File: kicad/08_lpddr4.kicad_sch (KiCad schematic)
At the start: 42 parts, among them U501 Ti135N484I3, U801 H9HCNNN8KUMLHR-NME

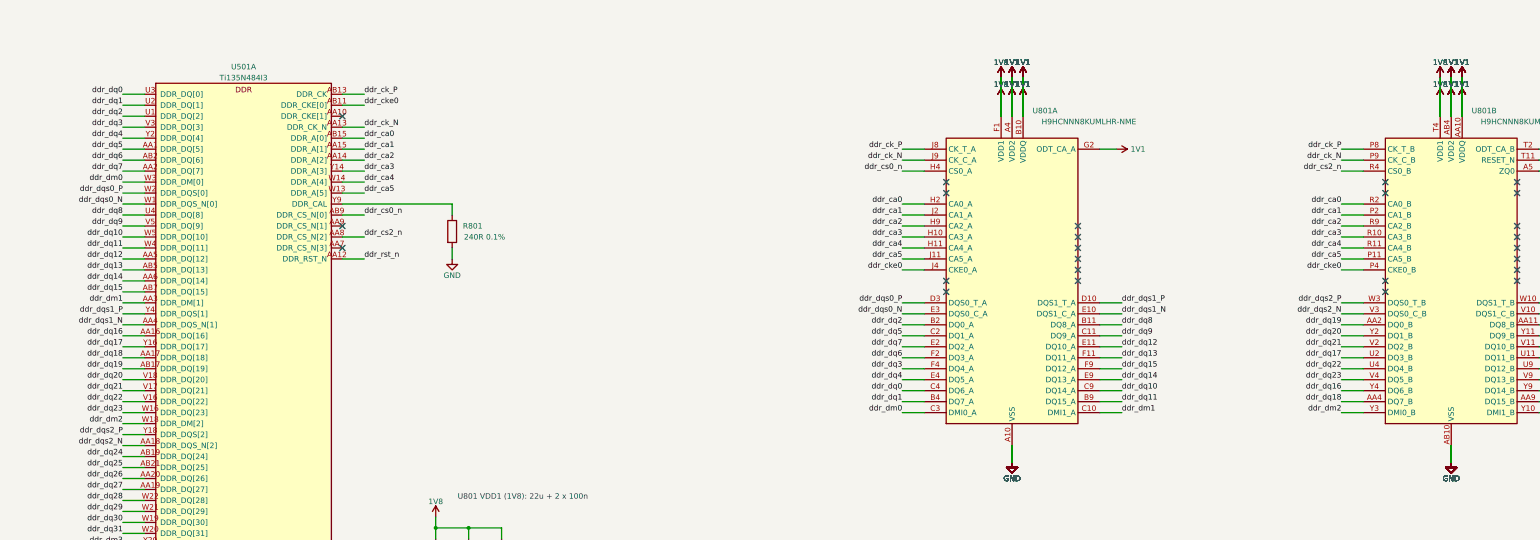
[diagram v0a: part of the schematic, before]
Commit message: LPDDR4 hand routing: Agilex DRAM escape copied, byte lanes routed, DQ swizzle by hand
- U801 decoupling = the Agilex U12 set (sheet 08: 29 x 100n 0201, 22u/1u 0402, LCSC from the
  Agilex card), placed at the Agilex positions on the same via pairs; R802 (ZQ) at R43's spot;
  CA/CKE T-branches on B.Cu copied (tools/ddr/copy_dram_escape.py)
- LPDDR4 vias not on a BGA ball removed (T-branch centre vias kept)
- Schematic: #PWR/#FLG references made unique per sheet (prefix = sheet number); the
  duplicates blocked Update PCB from Schematic
- DQ swizzle now edited by hand in the schematic (bytes 0 and 2); efinity/pinplan/lpddr4_swizzle.json
  is not updated yet
- Byte lanes routed by hand (work in progress)

Known open (WIP): byte 2 - ddr_dq22 on two U501 balls (AA16, W16), ddr_dq21 has no U501 ball;
DRC shows 2 shorts at U501 Y16/W16 (dq21/dq17 tracks).

Co-Authored-By: Claude Opus 5.5 <noreply@anthropic.com>
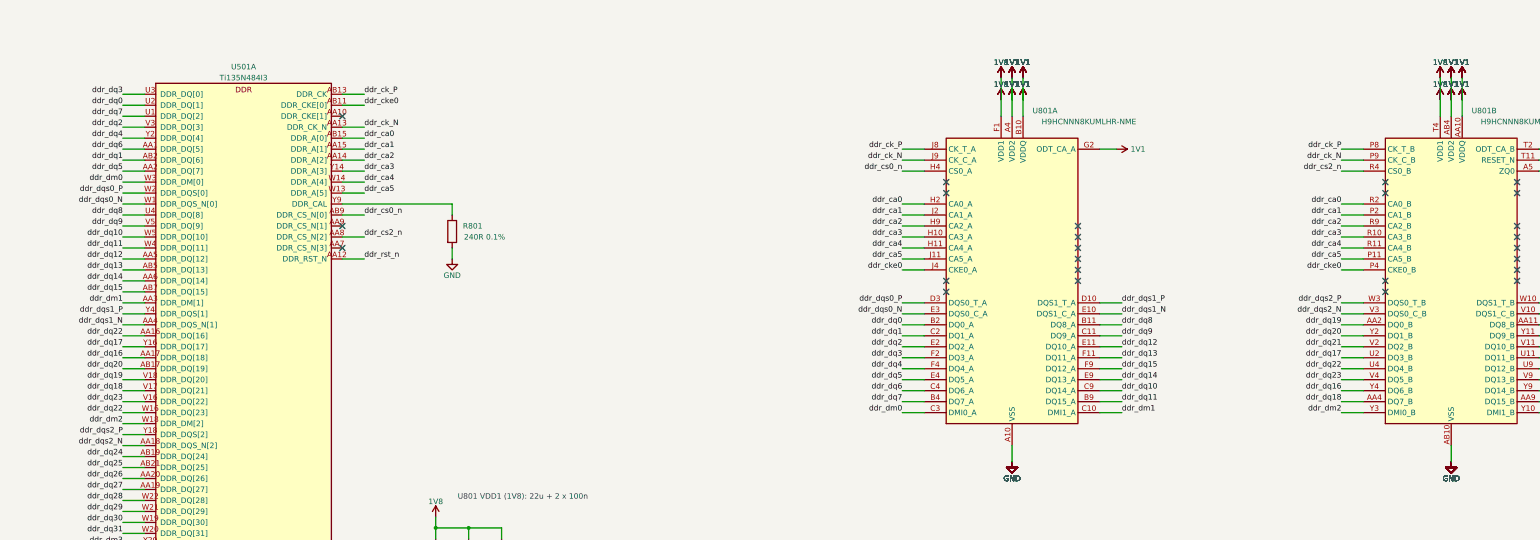
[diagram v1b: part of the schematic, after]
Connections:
- net ddr_dq0: now also U501.U2 (DDR_DQ[1]), U801.B2 (DQ0_A); no longer U501.U3 (DDR_DQ[0]), U801.C4 (DQ6_A)
- net ddr_dq1: now also U501.AB2 (DDR_DQ[6]), U801.C2 (DQ1_A); no longer U501.U2 (DDR_DQ[1]), U801.B4 (DQ7_A)
- net ddr_dq16: now also U501.AA17 (DDR_DQ[18]); no longer U501.AA16 (DDR_DQ[16])
- net ddr_dq18: now also U501.V17 (DDR_DQ[21]); no longer U501.AA17 (DDR_DQ[18])
- net ddr_dq19: now also U501.V18 (DDR_DQ[20]); no longer U501.AB17 (DDR_DQ[19])
- net ddr_dq2: now also U501.V3 (DDR_DQ[3]), U801.E2 (DQ2_A); no longer U501.U1 (DDR_DQ[2]), U801.B2 (DQ0_A)
- net ddr_dq20: now also U501.AB17 (DDR_DQ[19]); no longer U501.V18 (DDR_DQ[20])
- net ddr_dq21: no longer U501.V17 (DDR_DQ[21])
- net ddr_dq22: now also U501.AA16 (DDR_DQ[16]), U501.W16 (DDR_DQ[23]); no longer U501.V16 (DDR_DQ[22])
- net ddr_dq23: now also U501.V16 (DDR_DQ[22]); no longer U501.W16 (DDR_DQ[23])
- net ddr_dq3: now also U501.U3 (DDR_DQ[0]), U801.F2 (DQ3_A); no longer U501.V3 (DDR_DQ[3]), U801.F4 (DQ4_A)
- net ddr_dq4: now also U801.F4 (DQ4_A); no longer U801.E4 (DQ5_A)
- net ddr_dq5: now also U501.AA2 (DDR_DQ[7]), U801.E4 (DQ5_A); no longer U501.AA1 (DDR_DQ[5]), U801.C2 (DQ1_A)
- net ddr_dq6: now also U501.AA1 (DDR_DQ[5]), U801.C4 (DQ6_A); no longer U501.AB2 (DDR_DQ[6]), U801.F2 (DQ3_A)
- net ddr_dq7: now also U501.U1 (DDR_DQ[2]), U801.B4 (DQ7_A); no longer U501.AA2 (DDR_DQ[7]), U801.E2 (DQ2_A)

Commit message: LPDDR4: third byte lane routed; DQ nets named after the DRAM pins
- Byte 2 swizzle fixed in the schematic (U501 W16/Y16 labels), matching the copper;
  the two shorts at W16/Y16 are gone
- ddr_dq<n> = DRAM DQ<n>_A (n 0-15) / DQ<n-16>_B (n 16-31); the swizzle shows only at the
  FPGA pins. Labels and board nets renamed (22 nets in bytes 1-3), copper unchanged
- TI135_PCB_NOTES.md 6.1: naming note and FPGA ball -> DRAM bit table updated;
  efinity/pinplan/lpddr4_swizzle.json still holds the old map
- Third byte lane routed by hand (work in progress: DRC clearance/width/skew still open)

Co-Authored-By: Claude Opus 5.5 <noreply@anthropic.com>
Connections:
- net ddr_dq10: now also U501.AA5 (DDR_DQ[12]), U801.E11 (DQ10_A); no longer U501.W5 (DDR_DQ[10]), U801.C9 (DQ14_A)
- net ddr_dq11: now also U501.AB5 (DDR_DQ[13]), U801.F11 (DQ11_A); no longer U501.W4 (DDR_DQ[11]), U801.B9 (DQ15_A)
- net ddr_dq12: now also U501.AB7 (DDR_DQ[15]), U801.F9 (DQ12_A); no longer U501.AA5 (DDR_DQ[12]), U801.E11 (DQ10_A)
- net ddr_dq13: now also U501.AA6 (DDR_DQ[14]), U801.E9 (DQ13_A); no longer U501.AB5 (DDR_DQ[13]), U801.F11 (DQ11_A)
- net ddr_dq14: now also U501.W5 (DDR_DQ[10]), U801.C9 (DQ14_A); no longer U501.AA6 (DDR_DQ[14]), U801.E9 (DQ13_A)
- net ddr_dq15: now also U501.W4 (DDR_DQ[11]), U801.B9 (DQ15_A); no longer U501.AB7 (DDR_DQ[15]), U801.F9 (DQ12_A)
- net ddr_dq16: now also U501.V18 (DDR_DQ[20]), U801.AA2 (DQ0_B); no longer U501.AA17 (DDR_DQ[18]), U801.Y4 (DQ6_B)
- net ddr_dq17: now also U501.AB17 (DDR_DQ[19]), U801.Y2 (DQ1_B); no longer U501.Y16 (DDR_DQ[17]), U801.U2 (DQ3_B)
- net ddr_dq18: now also U501.Y16 (DDR_DQ[17]), U801.V2 (DQ2_B); no longer U501.V17 (DDR_DQ[21]), U801.AA4 (DQ7_B)
- net ddr_dq19: now also U501.W16 (DDR_DQ[23]), U801.U2 (DQ3_B); no longer U501.V18 (DDR_DQ[20]), U801.AA2 (DQ0_B)
- net ddr_dq20: now also U501.AA16 (DDR_DQ[16]), U801.U4 (DQ4_B); no longer U501.AB17 (DDR_DQ[19]), U801.Y2 (DQ1_B)
- net ddr_dq21: now also U501.V16 (DDR_DQ[22]), U801.V4 (DQ5_B); no longer U801.V2 (DQ2_B)
- net ddr_dq22: now also U501.AA17 (DDR_DQ[18]), U801.Y4 (DQ6_B); no longer U501.AA16 (DDR_DQ[16]), U501.W16 (DDR_DQ[23]), U801.U4 (DQ4_B)
- net ddr_dq23: now also U501.V17 (DDR_DQ[21]), U801.AA4 (DQ7_B); no longer U501.V16 (DDR_DQ[22]), U801.V4 (DQ5_B)
- net ddr_dq24: now also U501.W21 (DDR_DQ[29]), U801.AA11 (DQ8_B); no longer U501.AB19 (DDR_DQ[24]), U801.V9 (DQ13_B)
- net ddr_dq25: now also U501.AA20 (DDR_DQ[26]), U801.Y11 (DQ9_B); no longer U501.AB21 (DDR_DQ[25]), U801.AA9 (DQ15_B)
- net ddr_dq26: now also U501.AA19 (DDR_DQ[27]), U801.V11 (DQ10_B); no longer U501.AA20 (DDR_DQ[26]), U801.Y9 (DQ14_B)
- net ddr_dq27: now also U501.W19 (DDR_DQ[30]), U801.U11 (DQ11_B); no longer U501.AA19 (DDR_DQ[27]), U801.U9 (DQ12_B)
- net ddr_dq28: now also U501.W20 (DDR_DQ[31]), U801.U9 (DQ12_B); no longer U501.W22 (DDR_DQ[28]), U801.AA11 (DQ8_B)
- net ddr_dq29: now also U501.AB19 (DDR_DQ[24]), U801.V9 (DQ13_B); no longer U501.W21 (DDR_DQ[29]), U801.Y11 (DQ9_B)
- net ddr_dq30: now also U501.AB21 (DDR_DQ[25]), U801.Y9 (DQ14_B); no longer U501.W19 (DDR_DQ[30]), U801.U11 (DQ11_B)
- net ddr_dq31: now also U501.W22 (DDR_DQ[28]), U801.AA9 (DQ15_B); no longer U501.W20 (DDR_DQ[31]), U801.V11 (DQ10_B)
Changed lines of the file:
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@@
+		)
+	)
+	(label "ddr_dq27"
+		(at 60.96 182.88 180)
+		(effects
+			(font
+				(size 1.27 1.27)
+			)
+			(justify right bottom)
 		)
 	)
 	(label "ddr_dq30"
-		(at 60.96 182.88 180)
-		(effects
-			(font
-				(size 1.27 1.27)
-			)
-			(justify right bottom)
-		)
-	)
-	(label "ddr_dq25"
 		(at 60.96 170.18 180)
 		(effects
@@
 		)
 	)
-	(label "ddr_dq14"
+	(label "ddr_dq13"
 		(at 292.1 149.86 0)
 		(effects
@@
 		)
 	)
-	(label "ddr_dq31"
+	(label "ddr_dq28"
 		(at 60.96 185.42 180)
 		(effects
@@
 		)
 	)
-	(label "ddr_dq26"
+	(label "ddr_dq25"
 		(at 60.96 172.72 180)
 		(effects
@@
 		)
 	)
-	(label "ddr_dq18"
+	(label "ddr_dq23"
 		(at 342.9 154.94 180)
 		(effects
@@
 		)
 	)
-	(label "ddr_dq15"
+	(label "ddr_dq12"
 		(at 60.96 129.54 180)
 		(effects
@@
 		)
 	)
-	(label "ddr_dq18"
+	(label "ddr_dq23"
 		(at 60.96 152.4 180)
 		(effects
@@
 		)
 	)
-	(label "ddr_dq11"
+	(label "ddr_dq15"
 		(at 292.1 154.94 0)
 		(effects
@@
 		)
 	)
-	(label "ddr_dq22"
+	(label "ddr_dq19"
 		(at 60.96 157.48 180)
 		(effects
@@
 		)
 	)
-	(label "ddr_dq31"
+	(label "ddr_dq26"
 		(at 393.7 142.24 0)
 		(effects
@@
 		)
 	)
-	(label "ddr_dq19"
+	(label "ddr_dq16"
 		(at 60.96 149.86 180)
 		(effects
@@
 		)
 	)
-	(label "ddr_dq19"
+	(label "ddr_dq16"
 		(at 342.9 137.16 180)
 		(effects
@@
 		)
 	)
-	(label "ddr_dq12"
+	(label "ddr_dq10"
 		(at 60.96 121.92 180)
 		(effects
@@
 		)
 	)
-	(label "ddr_dq23"
+	(label "ddr_dq21"
 		(at 342.9 149.86 180)
 		(effects
@@
 		)
 	)
-	(label "ddr_dq14"
+	(label "ddr_dq13"
 		(at 60.96 127 180)
 		(effects
@@
 		)
 	)
-	(label "ddr_dq16"
+	(label "ddr_dq22"
 		(at 342.9 152.4 180)
 		(effects
@@
 		)
 	)
-	(label "ddr_dq10"
+	(label "ddr_dq14"
 		(at 292.1 152.4 0)
 		(effects
@@
 		)
 	)
-	(label "ddr_dq22"
+	(label "ddr_dq20"
 		(at 342.9 147.32 180)
 		(effects
@@
 		)
 	)
-	(label "ddr_dq20"
+	(label "ddr_dq17"
 		(at 342.9 139.7 180)
 		(effects
@@
 		)
 	)
-	(label "ddr_dq28"
+	(label "ddr_dq31"
 		(at 60.96 177.8 180)
 		(effects
@@
 		)
 	)
-	(label "ddr_dq11"
+	(label "ddr_dq15"
 		(at 60.96 119.38 180)
 		(effects
@@
 		)
 	)
-	(label "ddr_dq26"
+	(label "ddr_dq30"
 		(at 393.7 152.4 0)
 		(effects
@@
 		)
 	)
-	(label "ddr_dq13"
+	(label "ddr_dq11"
 		(at 60.96 124.46 180)
 		(effects
@@
 		)
 	)
-	(label "ddr_dq24"
+	(label "ddr_dq29"
 		(at 60.96 167.64 180)
 		(effects
@@
 		)
 	)
-	(label "ddr_dq16"
+	(label "ddr_dq22"
 		(at 60.96 144.78 180)
 		(effects
@@
 		)
 	)
-	(label "ddr_dq20"
+	(label "ddr_dq17"
 		(at 60.96 147.32 180)
 		(effects
@@
 		)
 	)
-	(label "ddr_dq23"
+	(label "ddr_dq21"
 		(at 60.96 154.94 180)
 		(effects
@@
 		)
 	)
-	(label "ddr_dq28"
+	(label "ddr_dq24"
 		(at 393.7 137.16 0)
 		(effects
@@
 		)
 	)
-	(label "ddr_dq24"
+	(label "ddr_dq29"
 		(at 393.7 149.86 0)
 		(effects
@@
 		)
 	)
-	(label "ddr_dq10"
+	(label "ddr_dq14"
 		(at 60.96 116.84 180)
 		(effects
@@
 		)
 	)
-	(label "ddr_dq13"
+	(label "ddr_dq11"
 		(at 292.1 144.78 0)
 		(effects
@@
 		)
 	)
-	(label "ddr_dq22"
+	(label "ddr_dq20"
 		(at 60.96 139.7 180)
 		(effects
@@
 		)
 	)
-	(label "ddr_dq17"
+	(label "ddr_dq18"
 		(at 60.96 142.24 180)
 		(effects
@@
 		)
 	)
-	(label "ddr_dq21"
+	(label "ddr_dq18"
 		(at 342.9 142.24 180)
 		(effects
@@
 		)
 	)
-	(label "ddr_dq27"
+	(label "ddr_dq26"
 		(at 60.96 175.26 180)
 		(effects
@@
 		)
 	)
-	(label "ddr_dq29"
+	(label "ddr_dq25"
 		(at 393.7 139.7 0)
 		(effects
@@
 		)
 	)
-	(label "ddr_dq25"
+	(label "ddr_dq31"
 		(at 393.7 154.94 0)
 		(effects
@@
 		)
 	)
-	(label "ddr_dq29"
+	(label "ddr_dq24"
 		(at 60.96 180.34 180)
 		(effects
@@
 		)
 	)
-	(label "ddr_dq17"
+	(label "ddr_dq19"
 		(at 342.9 144.78 180)
 		(effects
@@
 		)
 	)
-	(label "ddr_dq12"
+	(label "ddr_dq10"
 		(at 292.1 142.24 0)
 		(effects
@@
 		)
 	)
-	(label "ddr_dq30"
+	(label "ddr_dq27"
 		(at 393.7 144.78 0)
 		(effects
@@
 		)
 	)
-	(label "ddr_dq27"
+	(label "ddr_dq28"
 		(at 393.7 147.32 0)
 		(effects
@@
 		)
 	)
-	(label "ddr_dq15"
+	(label "ddr_dq12"
 		(at 292.1 147.32 0)
 		(effects

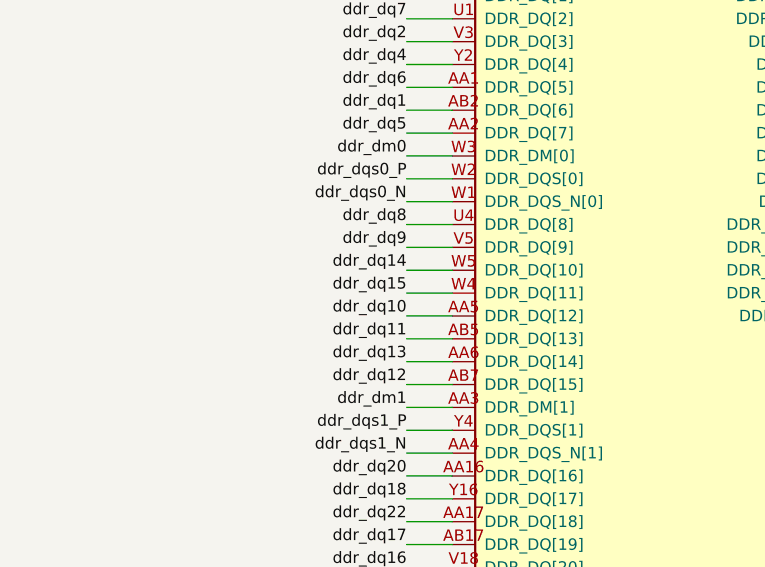
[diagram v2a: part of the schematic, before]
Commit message: LPDDR4: last byte lane routed; byte 1 DQ swizzle follows the layout
Byte 1 (FPGA DDR_DQ[15:8] -> DQ[15:8]_A) re-swizzled by hand in the schematic;
lpddr4_swizzle.json "1" = [7,1,5,0,6,2,3,4] (from the schematic netlist), Interface
Designer PIN_SWIZZLE_DQM1 regenerated by pinplan.py (design check passed),
TI135_PCB_NOTES byte 1 row updated. DRC: schematic parity 0, no clearance errors.

Co-Authored-By: Claude Opus 5.5 <noreply@anthropic.com>
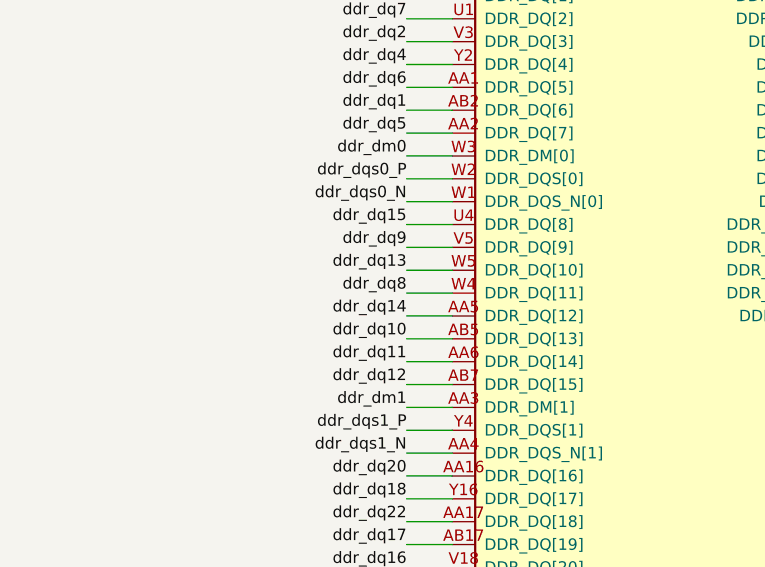
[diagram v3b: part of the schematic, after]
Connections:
- net ddr_dq10: now also U501.AB5 (DDR_DQ[13]); no longer U501.AA5 (DDR_DQ[12])
- net ddr_dq11: now also U501.AA6 (DDR_DQ[14]); no longer U501.AB5 (DDR_DQ[13])
- net ddr_dq13: now also U501.W5 (DDR_DQ[10]); no longer U501.AA6 (DDR_DQ[14])
- net ddr_dq14: now also U501.AA5 (DDR_DQ[12]); no longer U501.W5 (DDR_DQ[10])
- net ddr_dq15: now also U501.U4 (DDR_DQ[8]); no longer U501.W4 (DDR_DQ[11])
- net ddr_dq8: now also U501.W4 (DDR_DQ[11]); no longer U501.U4 (DDR_DQ[8])
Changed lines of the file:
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@@
 		)
 	)
-	(label "ddr_dq10"
+	(label "ddr_dq14"
 		(at 60.96 121.92 180)
 		(effects
@@
 		)
 	)
-	(label "ddr_dq13"
+	(label "ddr_dq11"
 		(at 60.96 127 180)
 		(effects
@@
 		)
 	)
-	(label "ddr_dq15"
+	(label "ddr_dq8"
 		(at 60.96 119.38 180)
 		(effects
@@
 		)
 	)
-	(label "ddr_dq11"
+	(label "ddr_dq10"
 		(at 60.96 124.46 180)
 		(effects
@@
 		)
 	)
-	(label "ddr_dq8"
+	(label "ddr_dq15"
 		(at 60.96 111.76 180)
 		(effects
@@
 		)
 	)
-	(label "ddr_dq14"
+	(label "ddr_dq13"
 		(at 60.96 116.84 180)
 		(effects

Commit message: LCSC numbers for all JLC parts; Y701 -> YXC OT322525MJBA4SL
- tools/set_lcsc.py: one table (value, footprint) -> LCSC, fills empty LCSC fields in the
  sheets; 312 symbols. JLC basic parts where available, cap voltages checked per rail,
  VCORE divider 0.1 % (no 0.5 % in stock). Board fields synced with add_parts.py.
- Y701: the SiT8924 has no JLC stock; now YXC OT322525MJBA4SL (C669088, 3225), EN tied
  to 1V8. R701/C701 moved 0.5 mm to clear its courtyard. Netlist change: Y701 pin 1 -> 1V8.
- Only U501 (Ti135) is left without LCSC (global sourcing / consigned).
- DRC: schematic parity 0.

Co-Authored-By: Claude Opus 5.5 <noreply@anthropic.com>
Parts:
- R802: LCSC (none) -> C25094
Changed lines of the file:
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@@
+			)
+		)
+		(property "LCSC" "C25094"
+			(at 406.4 101.6 0)
+			(effects
+				(font
+					(size 1.27 1.27)
+				)
+				(hide yes)
 			)
 		)
